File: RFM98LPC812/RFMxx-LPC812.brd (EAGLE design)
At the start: 60 x 38.7 mm, 39 parts, among them X1 BU-SMA-V, X2 BU-SMA-V

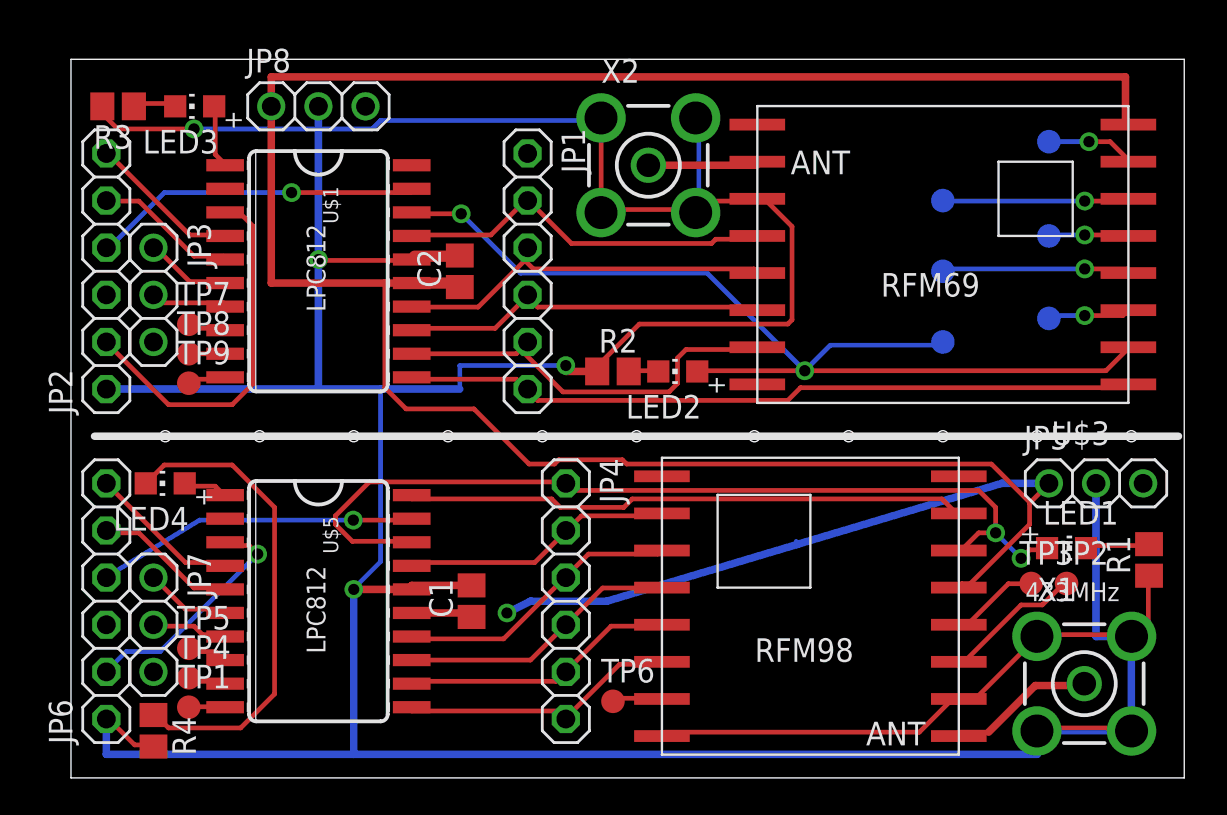
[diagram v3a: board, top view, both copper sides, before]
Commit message: better routing of power to RFM98
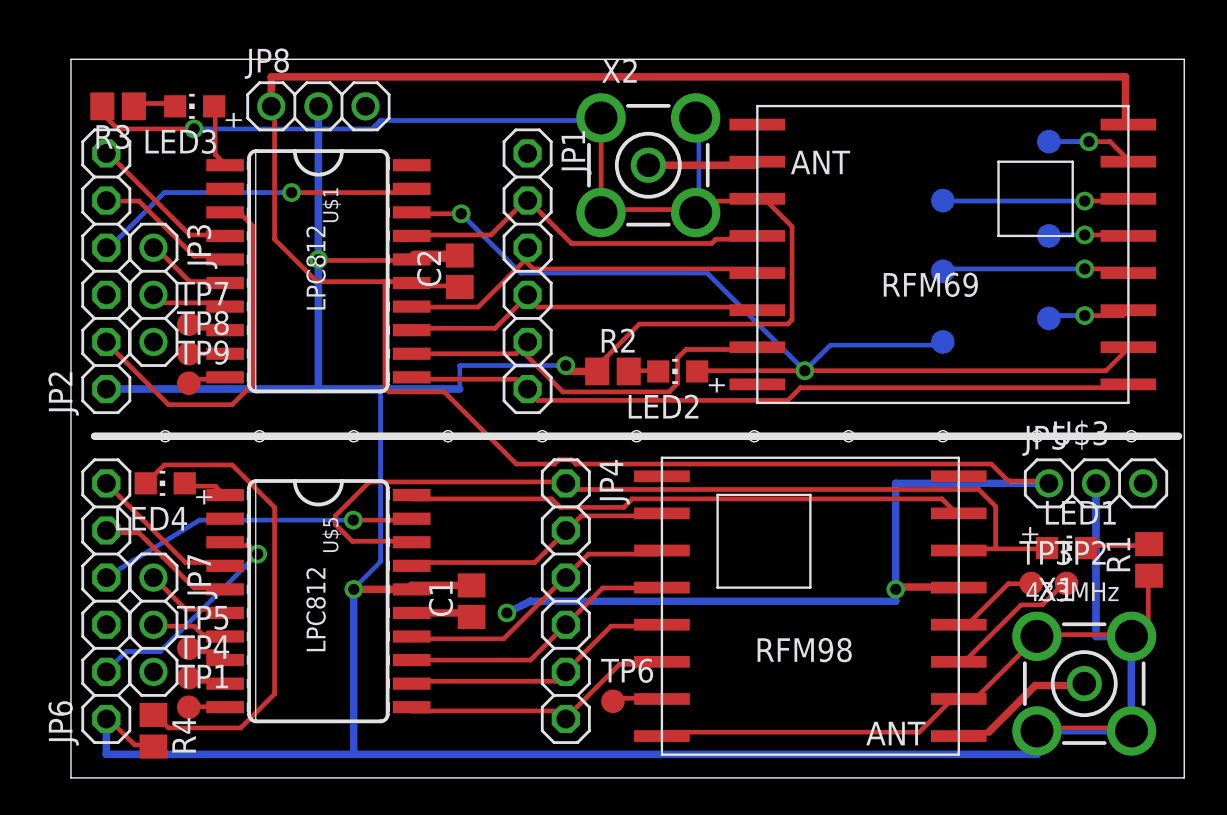
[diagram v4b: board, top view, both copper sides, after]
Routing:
- net VCC: track 152.1 -> 151.8 mm, vias 1 -> 2
- net N$22: track 49.3 -> 49.0 mm, vias 2 -> 0
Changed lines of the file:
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@@
 <contactref element="U$2" pad="VCC"/>
 <contactref element="JP5" pad="1"/>
-<wire x1="52.705" y1="15.875" x2="50.165" y2="15.875" width="0.4064" layer="16"/>
-<wire x1="50.165" y1="15.875" x2="39.140371875" y2="12.584065625" width="0.4064" layer="16"/>
-<wire x1="39.140371875" y1="12.584065625" x2="28.8925" y2="9.525" width="0.4064" layer="16"/>
-<wire x1="28.8925" y1="9.525" x2="24.765" y2="9.525" width="0.4064" layer="16"/>
 <wire x1="24.765" y1="9.525" x2="23.495" y2="8.89" width="0.4064" layer="16"/>
 <via x="23.495" y="8.89" extent="1-16" drill="0.6"/>
@@
 <contactref element="C2" pad="1"/>
 <contactref element="JP8" pad="1"/>
-<wire x1="39.0906" y1="12.7508" x2="39.140371875" y2="12.584065625" width="0.254" layer="16"/>
 <wire x1="10.795" y1="36.195" x2="10.795" y2="37.7825" width="0.4064" layer="1"/>
 <wire x1="10.795" y1="37.7825" x2="56.8325" y2="37.7825" width="0.4064" layer="1"/>
@@
 <wire x1="56.9214" y1="35.2044" x2="56.8325" y2="35.2425" width="0.254" layer="1"/>
 <wire x1="52.578" y1="15.9512" x2="52.705" y2="15.875" width="0.254" layer="1"/>
-<wire x1="48.4632" y1="10.4648" x2="48.006" y2="10.4648" width="0.254" layer="1"/>
-<wire x1="51.6636" y1="13.6652" x2="48.4632" y2="10.4648" width="0.254" layer="1"/>
-<wire x1="51.6636" y1="14.8082" x2="51.6636" y2="13.6652" width="0.254" layer="1"/>
-<wire x1="52.578" y1="15.7226" x2="51.689" y2="14.8336" width="0.254" layer="1"/>
-<wire x1="51.689" y1="14.8336" x2="51.6636" y2="14.8082" width="0.254" layer="1"/>
-<wire x1="48.006" y1="10.4648" x2="47.85" y2="10.255" width="0.254" layer="1"/>
-<wire x1="52.578" y1="15.7226" x2="52.705" y2="15.875" width="0.254" layer="1"/>
-<wire x1="10.795" y1="36.195" x2="10.795" y2="26.67" width="0.4064" layer="1"/>
-<wire x1="20.955" y1="26.67" x2="18.415" y2="26.67" width="0.6096" layer="1"/>
-<wire x1="10.795" y1="26.67" x2="16.9164" y2="26.67" width="0.4064" layer="1"/>
-<wire x1="16.9164" y1="26.67" x2="18.288" y2="26.67" width="0.4064" layer="1"/>
-<wire x1="18.288" y1="26.67" x2="18.3642" y2="26.67" width="0.4064" layer="1"/>
-<wire x1="18.3642" y1="26.67" x2="18.415" y2="26.67" width="0.4064" layer="1"/>
-<wire x1="21.0312" y1="26.5176" x2="20.955" y2="26.455" width="0.254" layer="1"/>
-<wire x1="21.0312" y1="26.5176" x2="20.955" y2="26.67" width="0.254" layer="1"/>
-<wire x1="18.288" y1="26.7462" x2="18.288" y2="26.67" width="0.254" layer="1"/>
+<wire x1="24.765" y1="9.525" x2="44.45" y2="9.525" width="0.4064" layer="16"/>
+<wire x1="44.45" y1="9.525" x2="44.45" y2="10.16" width="0.4064" layer="16"/>
+<wire x1="44.45" y1="10.16" x2="44.45" y2="15.875" width="0.4064" layer="16"/>
+<wire x1="44.45" y1="15.875" x2="52.705" y2="15.875" width="0.4064" layer="16"/>
+<wire x1="18.5166" y1="26.5176" x2="20.8026" y2="26.5176" width="0.254" layer="1"/>
+<wire x1="20.8026" y1="26.5176" x2="20.955" y2="26.455" width="0.254" layer="1"/>
+<wire x1="18.5166" y1="26.5176" x2="18.3642" y2="26.67" width="0.254" layer="1"/>
+<wire x1="13.2588" y1="26.7462" x2="16.9164" y2="26.7462" width="0.254" layer="1"/>
+<wire x1="16.9164" y1="26.7462" x2="18.288" y2="26.7462" width="0.254" layer="1"/>
+<wire x1="10.9728" y1="29.0322" x2="13.2588" y2="26.7462" width="0.254" layer="1"/>
+<wire x1="10.9728" y1="36.1188" x2="10.9728" y2="29.0322" width="0.254" layer="1"/>
 <wire x1="18.288" y1="26.7462" x2="18.3642" y2="26.67" width="0.254" layer="1"/>
-<wire x1="16.9164" y1="21.0312" x2="16.9164" y2="26.67" width="0.254" layer="1"/>
-<wire x1="18.0594" y1="19.8882" x2="16.9164" y2="21.0312" width="0.254" layer="1"/>
-<wire x1="21.717" y1="19.8882" x2="18.0594" y2="19.8882" width="0.254" layer="1"/>
-<wire x1="24.6888" y1="16.9164" x2="21.717" y2="19.8882" width="0.254" layer="1"/>
-<wire x1="26.0604" y1="16.9164" x2="24.6888" y2="16.9164" width="0.254" layer="1"/>
-<wire x1="26.289" y1="17.145" x2="26.0604" y2="16.9164" width="0.254" layer="1"/>
-<wire x1="29.718" y1="17.145" x2="26.289" y2="17.145" width="0.254" layer="1"/>
-<wire x1="29.9466" y1="16.9164" x2="29.718" y2="17.145" width="0.254" layer="1"/>
-<wire x1="49.6062" y1="16.9164" x2="29.9466" y2="16.9164" width="0.254" layer="1"/>
-<wire x1="51.689" y1="14.8336" x2="49.6062" y2="16.9164" width="0.254" layer="1"/>
+<wire x1="10.9728" y1="36.1188" x2="10.795" y2="36.195" width="0.254" layer="1"/>
+<wire x1="50.5206" y1="16.002" x2="52.578" y2="16.002" width="0.254" layer="1"/>
+<wire x1="49.6062" y1="16.9164" x2="50.5206" y2="16.002" width="0.254" layer="1"/>
+<wire x1="27.2034" y1="16.9164" x2="49.6062" y2="16.9164" width="0.254" layer="1"/>
+<wire x1="26.9748" y1="17.145" x2="27.2034" y2="16.9164" width="0.254" layer="1"/>
+<wire x1="26.289" y1="17.145" x2="26.9748" y2="17.145" width="0.254" layer="1"/>
+<wire x1="26.0604" y1="16.9164" x2="26.289" y2="17.145" width="0.254" layer="1"/>
+<wire x1="24.003" y1="16.9164" x2="26.0604" y2="16.9164" width="0.254" layer="1"/>
+<wire x1="20.1168" y1="20.8026" x2="24.003" y2="16.9164" width="0.254" layer="1"/>
+<wire x1="17.145" y1="20.8026" x2="20.1168" y2="20.8026" width="0.254" layer="1"/>
+<wire x1="16.9164" y1="21.0312" x2="17.145" y2="20.8026" width="0.254" layer="1"/>
+<wire x1="16.9164" y1="26.7462" x2="16.9164" y2="21.0312" width="0.254" layer="1"/>
+<wire x1="52.578" y1="16.002" x2="52.705" y2="15.875" width="0.254" layer="1"/>
+<via x="44.45" y="10.16" extent="1-16" drill="0.6"/>
+<wire x1="44.577" y1="10.287" x2="47.7774" y2="10.287" width="0.4064" layer="1"/>
+<wire x1="47.7774" y1="10.287" x2="47.85" y2="10.255" width="0.254" layer="1"/>
+<wire x1="44.577" y1="10.287" x2="44.45" y2="10.16" width="0.254" layer="1"/>
 </signal>
 <signal name="N$6">
@@
 <wire x1="26.5938" y1="15.9512" x2="26.67" y2="15.875" width="0.254" layer="1"/>
 <contactref element="LED1" pad="A"/>
-<wire x1="51.6636" y1="12.2936" x2="52.578" y2="12.2936" width="0.254" layer="1"/>
-<wire x1="51.2064" y1="11.8364" x2="51.6636" y2="12.2936" width="0.254" layer="1"/>
-<wire x1="49.8348" y1="13.208" x2="51.2064" y2="11.8364" width="0.254" layer="16"/>
-<wire x1="48.9204" y1="13.208" x2="49.8348" y2="13.208" width="0.254" layer="1"/>
-<wire x1="48.006" y1="12.2936" x2="48.9204" y2="13.208" width="0.254" layer="1"/>
-<wire x1="52.578" y1="12.2936" x2="52.6075" y2="12.3825" width="0.254" layer="1"/>
-<wire x1="48.006" y1="12.2936" x2="47.85" y2="12.255" width="0.254" layer="1"/>
-<wire x1="49.8348" y1="14.5796" x2="49.8348" y2="13.208" width="0.254" layer="1"/>
-<wire x1="48.9204" y1="15.494" x2="49.8348" y2="14.5796" width="0.254" layer="1"/>
-<wire x1="26.9748" y1="15.494" x2="48.9204" y2="15.494" width="0.254" layer="1"/>
-<wire x1="26.7462" y1="15.7226" x2="26.9748" y2="15.494" width="0.254" layer="1"/>
-<wire x1="26.7462" y1="15.7226" x2="26.67" y2="15.875" width="0.254" layer="1"/>
-<via x="51.2064" y="11.8364" extent="1-16" drill="0.6096"/>
-<via x="49.8348" y="13.208" extent="1-16" drill="0.6096"/>
+<wire x1="48.006" y1="12.3444" x2="49.8348" y2="12.3444" width="0.254" layer="1"/>
+<wire x1="49.8348" y1="12.3444" x2="52.578" y2="12.3444" width="0.254" layer="1"/>
+<wire x1="52.578" y1="12.3444" x2="52.6075" y2="12.3825" width="0.254" layer="1"/>
+<wire x1="48.006" y1="12.3444" x2="47.85" y2="12.255" width="0.254" layer="1"/>
+<wire x1="49.8348" y1="14.6304" x2="49.8348" y2="12.3444" width="0.254" layer="1"/>
+<wire x1="48.9204" y1="15.5448" x2="49.8348" y2="14.6304" width="0.254" layer="1"/>
+<wire x1="26.9748" y1="15.5448" x2="48.9204" y2="15.5448" width="0.254" layer="1"/>
+<wire x1="26.7462" y1="15.7734" x2="26.9748" y2="15.5448" width="0.254" layer="1"/>
+<wire x1="26.7462" y1="15.7734" x2="26.67" y2="15.875" width="0.254" layer="1"/>
 </signal>
 <signal name="N$25">

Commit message: some refinements
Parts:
- added D_0, D_1, P14, TP12: TPB1,27, testpad:B1,27
- renumbered DIO0 to D0, DIO1 to D1, DIO2 to D2, DIO3 to D3, DIO4 to D4, DIO5 to D5, TP6 to D_5
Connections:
- removed net N$45: C1.2, U$5.16
- new net N$52: TP12.TP, U$2.DIO2
- net GND: now also C1.2, U$5.16
- net N$22: now also D_0.TP
- net N$27: now also D_1.TP
- net N$46: now also P14.TP, U$1.20; no longer C1.1, U$5.15
- net VCC: now also C1.1, U$5.15
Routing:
- net VCC: track 151.8 -> 121.7 mm
- net N$27: track 30.4 -> 54.6 mm, vias 0 -> 1
- net GND: track 256.3 -> 241.4 mm
- net N$22: track 49.0 -> 44.1 mm, vias 0 -> 1
- net N$52: track 0.00 -> 4.23 mm
- net N$45: track 3.44 -> 5.08 mm
- net N$46: track 3.44 -> 2.91 mm
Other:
- board text added: "RFM69/98 experimentation board Joe Desbonnet, jdesbonnet@gmail.com Revision 1. 7 Nov 2014"

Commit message: some tidyup before Rev 1
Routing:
- net GND: track 241.4 -> 224.3 mm
- net N$14: track 23.0 -> 19.7 mm
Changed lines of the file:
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@@
 <text x="59.3725" y="38.1" size="0.6096" layer="22" rot="MR270">RFM69/98 experimentation board
 Joe Desbonnet, jdesbonnet@gmail.com
-Revision 1. 7 Nov 2014</text>
+Revision 1.
+7 Nov 2014</text>
+<text x="36.83" y="38.1" size="1.016" layer="21" rot="R180">433MHz</text>
 </plain>
 <attributes>
@@
 <wire x1="42.2275" y1="15.875" x2="42.2275" y2="10.16" width="0.6096" layer="16"/>
 <wire x1="42.2275" y1="10.16" x2="42.2275" y2="9.525" width="0.6096" layer="16"/>
-<wire x1="42.2275" y1="9.525" x2="23.8125" y2="9.525" width="0.6096" layer="16"/>
 <via x="23.495" y="8.89" extent="1-16" drill="0.6"/>
 <wire x1="23.8125" y1="9.525" x2="23.495" y2="8.89" width="0.6096" layer="16"/>
@@
 <wire x1="10.9728" y1="26.8097" x2="18.3642" y2="26.8097" width="0.6096" layer="1"/>
 <wire x1="18.3642" y1="26.8097" x2="18.3642" y2="26.67" width="0.4064" layer="1"/>
+<wire x1="29.21" y1="9.525" x2="23.8125" y2="9.525" width="0.4064" layer="16"/>
+<wire x1="42.2275" y1="9.525" x2="29.21" y2="9.525" width="0.6096" layer="16"/>
 <wire x1="23.8125" y1="9.525" x2="20.955" y2="26.455" width="0" layer="19" extent="1-16"/>
 </signal>
@@
 <wire x1="24.2316" y1="23.0886" x2="24.003" y2="22.86" width="0.254" layer="1"/>
 <wire x1="24.4602" y1="23.3172" x2="24.61" y2="23.495" width="0.254" layer="1"/>
-<wire x1="36.8046" y1="23.3172" x2="36.99" y2="23.21" width="0.254" layer="1"/>
-<wire x1="24.6888" y1="23.3172" x2="24.61" y2="23.495" width="0.254" layer="1"/>
-<wire x1="33.147" y1="23.0886" x2="36.8046" y2="23.0886" width="0.254" layer="1"/>
-<wire x1="32.6898" y1="22.6314" x2="33.147" y2="23.0886" width="0.254" layer="1"/>
-<wire x1="32.6898" y1="21.2598" x2="32.6898" y2="22.6314" width="0.254" layer="1"/>
-<wire x1="32.2326" y1="20.8026" x2="32.6898" y2="21.2598" width="0.254" layer="1"/>
-<wire x1="26.5176" y1="20.8026" x2="32.2326" y2="20.8026" width="0.254" layer="1"/>
-<wire x1="24.2316" y1="23.0886" x2="26.5176" y2="20.8026" width="0.254" layer="1"/>
 <wire x1="36.8046" y1="23.0886" x2="36.99" y2="23.21" width="0.254" layer="1"/>
 <wire x1="24.2316" y1="23.0886" x2="24.61" y2="23.495" width="0.254" layer="1"/>
+<wire x1="24.61" y1="23.495" x2="36.99" y2="23.495" width="0.254" layer="1"/>
+<wire x1="36.99" y1="23.495" x2="36.99" y2="23.21" width="0" layer="19" extent="1-16"/>
 </signal>
 <signal name="N$15">
@@
 <via x="13.335" y="27.94" extent="1-16" drill="0.6"/>
 <wire x1="13.335" y1="20.955" x2="1.905" y2="20.955" width="0.4064" layer="16"/>
-<wire x1="28.575" y1="35.433" x2="28.575" y2="30.6324" width="0.254" layer="1"/>
+<wire x1="28.575" y1="35.433" x2="28.575" y2="30.6324" width="0.4064" layer="1"/>
 <wire x1="28.575" y1="35.433" x2="28.5676" y2="35.5699" width="0.254" layer="1"/>
-<wire x1="34.29" y1="31.0896" x2="36.8046" y2="31.0896" width="0.254" layer="1"/>
-<wire x1="33.8328" y1="30.6324" x2="34.29" y2="31.0896" width="0.254" layer="1"/>
+<wire x1="34.29" y1="31.0896" x2="36.8046" y2="31.0896" width="0.4064" layer="1"/>
+<wire x1="33.8328" y1="30.6324" x2="34.29" y2="31.0896" width="0.4064" layer="1"/>
 <wire x1="36.8046" y1="31.0896" x2="36.99" y2="31.21" width="0.254" layer="1"/>
 <wire x1="33.8328" y1="30.6324" x2="33.6674" y2="30.4701" width="0.254" layer="1"/>
-<wire x1="33.6042" y1="30.6324" x2="28.575" y2="30.6324" width="0.254" layer="1"/>
+<wire x1="33.6042" y1="30.6324" x2="28.575" y2="30.6324" width="0.4064" layer="1"/>
 <wire x1="28.575" y1="30.6324" x2="28.5676" y2="30.4701" width="0.254" layer="1"/>
 <wire x1="33.6042" y1="30.6324" x2="33.6674" y2="30.4701" width="0.254" layer="1"/>
-<wire x1="16.6878" y1="35.433" x2="28.3464" y2="35.433" width="0.254" layer="16"/>
-<wire x1="16.2306" y1="34.9758" x2="16.6878" y2="35.433" width="0.254" layer="16"/>
-<wire x1="13.335" y1="34.9758" x2="16.2306" y2="34.9758" width="0.254" layer="16"/>
-<wire x1="28.3464" y1="35.433" x2="28.5676" y2="35.5699" width="0.254" layer="16"/>
+<wire x1="13.335" y1="34.9758" x2="27.0256" y2="34.9758" width="0.254" layer="16"/>
 <wire x1="13.4874" y1="27.8892" x2="18.288" y2="27.8892" width="0.6096" layer="1"/>
 <wire x1="13.4874" y1="27.8892" x2="13.335" y2="27.94" width="0.254" layer="1"/>
@@
 <wire x1="1.8288" y1="36.1188" x2="1.69" y2="36.195" width="0.254" layer="1"/>
 <via x="6.6294" y="34.9758" extent="1-16" drill="0.6096"/>
-<wire x1="13.335" y1="20.955" x2="16.6878" y2="20.955" width="0" layer="19" extent="1-16"/>
 <wire x1="13.335" y1="20.955" x2="20.955" y2="20.955" width="0.4064" layer="16"/>
 <wire x1="20.955" y1="20.955" x2="20.955" y2="22.225" width="0.254" layer="16"/>
@@
 <contactref element="R4" pad="2"/>
 <wire x1="15.24" y1="1.27" x2="15.24" y2="10.16" width="0.4064" layer="16"/>
-<wire x1="33.8328" y1="30.6324" x2="33.8328" y2="35.433" width="0" layer="19" extent="1-16"/>
-<wire x1="33.8328" y1="35.433" x2="33.6674" y2="35.5699" width="0" layer="19" extent="1-16"/>
 <wire x1="33.8328" y1="30.6324" x2="33.6674" y2="30.4701" width="0.254" layer="16"/>
 <wire x1="4.3434" y1="1.8288" x2="4.445" y2="1.69" width="0.254" layer="1"/>
@@
 <wire x1="57.15" y1="7.7724" x2="57.1599" y2="7.6299" width="0.254" layer="16"/>
 <wire x1="57.15" y1="7.7724" x2="57.15" y2="7.62" width="0.254" layer="16"/>
-<wire x1="28.36" y1="21.9075" x2="26.67" y2="21.9075" width="0" layer="19" extent="1-16"/>
-<wire x1="26.67" y1="21.9075" x2="26.67" y2="22.225" width="0" layer="19" extent="1-16"/>
 <via x="15.24" y="10.16" extent="1-16" drill="0.6"/>
 <wire x1="15.24" y1="10.16" x2="18.288" y2="10.16" width="0.4064" layer="1"/>
 <wire x1="18.288" y1="10.16" x2="18.3642" y2="10.16" width="0.4064" layer="1"/>
 <wire x1="18.3642" y1="10.16" x2="18.415" y2="10.16" width="0.4064" layer="1"/>
-<wire x1="28.575" y1="22.4028" x2="28.575" y2="21.9456" width="0.254" layer="1"/>
-<wire x1="30.6324" y1="24.4602" x2="28.575" y2="22.4028" width="0.254" layer="1"/>
-<wire x1="38.6334" y1="24.4602" x2="30.6324" y2="24.4602" width="0.254" layer="1"/>
-<wire x1="38.862" y1="24.6888" x2="38.6334" y2="24.4602" width="0.254" layer="1"/>
-<wire x1="38.862" y1="29.718" x2="38.862" y2="24.6888" width="0.254" layer="1"/>
-<wire x1="37.4904" y1="31.0896" x2="38.862" y2="29.718" width="0.254" layer="1"/>
-<wire x1="37.0332" y1="31.0896" x2="37.4904" y2="31.0896" width="0.254" layer="1"/>
-<wire x1="28.575" y1="21.9456" x2="28.36" y2="21.9075" width="0.254" layer="1"/>
-<wire x1="37.0332" y1="31.0896" x2="36.99" y2="31.21" width="0.254" layer="1"/>
-<wire x1="16.6878" y1="11.6586" x2="16.6878" y2="20.955" width="0" layer="19" extent="1-16"/>
-<wire x1="15.3162" y1="10.287" x2="16.6878" y2="11.6586" width="0" layer="19" extent="1-16"/>
 <wire x1="15.3162" y1="10.287" x2="15.24" y2="10.16" width="0.254" layer="16"/>
 <contactref element="C1" pad="2"/>
@@
 <wire x1="18.288" y1="10.0584" x2="18.3642" y2="10.16" width="0.254" layer="1"/>
 <wire x1="18.288" y1="10.0584" x2="18.288" y2="10.16" width="0.254" layer="1"/>
+<wire x1="28.36" y1="21.9075" x2="26.67" y2="21.9075" width="0.4064" layer="1"/>
+<wire x1="26.67" y1="21.9075" x2="26.67" y2="22.225" width="0.4064" layer="1"/>
+<wire x1="27.0256" y1="34.9758" x2="28.5676" y2="34.9758" width="0.4064" layer="16"/>
+<wire x1="28.5676" y1="34.9758" x2="28.5676" y2="35.5699" width="0.4064" layer="16"/>
+<wire x1="34.29" y1="31.0896" x2="33.6674" y2="35.5699" width="0" layer="19" extent="1-1"/>
+<wire x1="26.67" y1="22.225" x2="26.67" y2="22.225" width="0" layer="19" extent="1-16"/>
+<wire x1="21.59" y1="10.375" x2="20.955" y2="20.955" width="0" layer="19" extent="1-16"/>
 </signal>
 <signal name="N$11">
